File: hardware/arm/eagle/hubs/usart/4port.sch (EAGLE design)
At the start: 15 parts

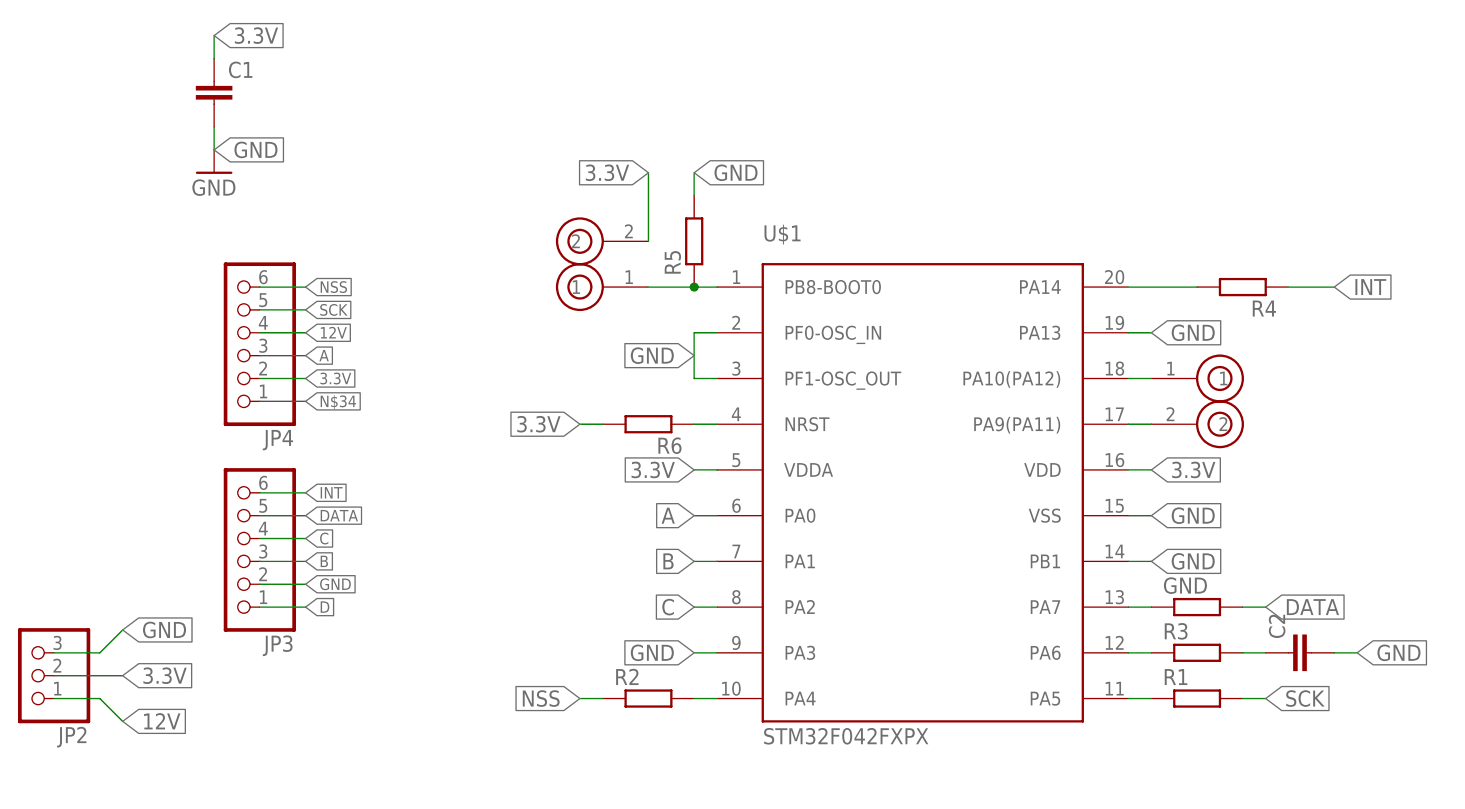
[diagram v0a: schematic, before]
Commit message: updated uart hub pcb
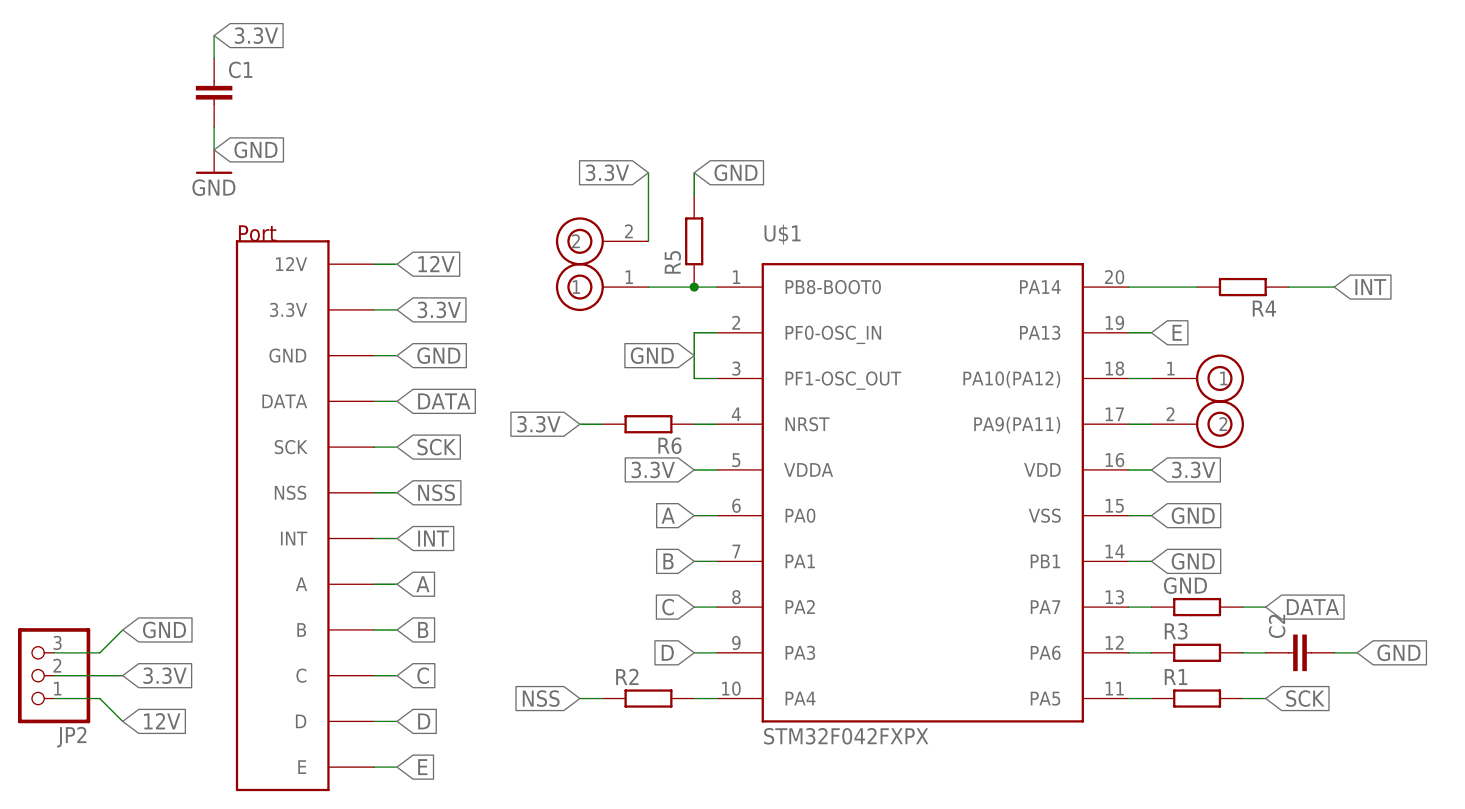
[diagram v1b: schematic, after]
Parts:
- removed JP3, JP4: (no value), pinhead:PINHD-1X6
- added U$4: HUB_PORT, gumyns:HUB_PORT
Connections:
- removed net N$34: JP4.1
- new net E: U$1.PA13, U$4.E
- net 12V: now also U$4.12V; no longer JP4.4
- net 3.3V: now also U$4.3.3V; no longer JP4.2
- net A: now also U$4.A; no longer JP4.3
- net B: now also U$4.B; no longer JP3.3
- net C: now also U$4.C; no longer JP3.4
- net D: now also U$1.PA3, U$4.D; no longer JP3.1
- net DATA: now also U$4.DATA; no longer JP3.5
- net GND: now also U$4.GND; no longer JP3.2, U$1.PA13, U$1.PA3
- net INT: now also U$4.INT; no longer JP3.6
- net NSS: now also U$4.NSS; no longer JP4.6
- net SCK: now also U$4.SCK; no longer JP4.5
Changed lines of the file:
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@@
 <?xml version="1.0" encoding="utf-8"?>
 <!DOCTYPE eagle SYSTEM "eagle.dtd">
-<eagle version="7.7.0">
+<eagle version="7.6.0">
 <drawing>
 <settings>
@@
 <part name="C2" library="resistor" deviceset="C-EU" device="C1206"/>
 <part name="R4" library="resistor" deviceset="R-EU_" device="R0603"/>
-<part name="JP3" library="pinhead" deviceset="PINHD-1X6" device=""/>
-<part name="JP4" library="pinhead" deviceset="PINHD-1X6" device=""/>
+<part name="U$4" library="gumyns" deviceset="HUB_PORT" device=""/>
 </parts>
 <sheets>
@@
 <instance part="C2" gate="G$1" x="142.24" y="63.5" rot="R90"/>
 <instance part="R4" gate="G$1" x="137.16" y="104.14" rot="R180"/>
-<instance part="JP3" gate="A" x="25.4" y="76.2" rot="R180"/>
-<instance part="JP4" gate="A" x="25.4" y="99.06" rot="R180"/>
+<instance part="U$4" gate="G$2" x="33.02" y="76.2"/>
 </instances>
 <busses>
@@
 </segment>
 <segment>
-<pinref part="JP4" gate="A" pin="4"/>
-<wire x1="27.94" y1="99.06" x2="33.02" y2="99.06" width="0.1524" layer="91"/>
-<label x="33.02" y="99.06" size="1.27" layer="95" xref="yes"/>
+<pinref part="U$4" gate="G$2" pin="12V"/>
+<wire x1="40.64" y1="106.68" x2="43.18" y2="106.68" width="0.1524" layer="91"/>
+<label x="43.18" y="106.68" size="1.778" layer="95" xref="yes"/>
 </segment>
 </net>
@@
 </segment>
 <segment>
-<pinref part="JP4" gate="A" pin="2"/>
-<wire x1="27.94" y1="93.98" x2="33.02" y2="93.98" width="0.1524" layer="91"/>
-<label x="33.02" y="93.98" size="1.27" layer="95" xref="yes"/>
+<pinref part="U$4" gate="G$2" pin="3.3V"/>
+<wire x1="40.64" y1="101.6" x2="43.18" y2="101.6" width="0.1524" layer="91"/>
+<label x="43.18" y="101.6" size="1.778" layer="95" xref="yes"/>
 </segment>
 </net>
@@
 </segment>
 <segment>
-<pinref part="U$1" gate="G$1" pin="PA13"/>
-<wire x1="124.46" y1="99.06" x2="127" y2="99.06" width="0.1524" layer="91"/>
-<label x="127" y="99.06" size="1.778" layer="95" xref="yes"/>
-</segment>
-<segment>
 <pinref part="U$1" gate="G$1" pin="VSS"/>
 <wire x1="124.46" y1="78.74" x2="127" y2="78.74" width="0.1524" layer="91"/>
@@
 </segment>
 <segment>
-<pinref part="U$1" gate="G$1" pin="PA3"/>
-<wire x1="78.74" y1="63.5" x2="76.2" y2="63.5" width="0.1524" layer="91"/>
-<label x="76.2" y="63.5" size="1.778" layer="95" rot="R180" xref="yes"/>
-</segment>
-<segment>
 <pinref part="R5" gate="G$1" pin="2"/>
 <wire x1="76.2" y1="114.3" x2="76.2" y2="116.84" width="0.1524" layer="91"/>
@@
 </segment>
 <segment>
-<pinref part="JP3" gate="A" pin="2"/>
-<wire x1="27.94" y1="71.12" x2="33.02" y2="71.12" width="0.1524" layer="91"/>
-<label x="33.02" y="71.12" size="1.27" layer="95" xref="yes"/>
+<pinref part="U$4" gate="G$2" pin="GND"/>
+<wire x1="40.64" y1="96.52" x2="43.18" y2="96.52" width="0.1524" layer="91"/>
+<label x="43.18" y="96.52" size="1.778" layer="95" xref="yes"/>
 </segment>
 </net>
@@
 </segment>
 <segment>
-<pinref part="JP4" gate="A" pin="6"/>
-<wire x1="27.94" y1="104.14" x2="33.02" y2="104.14" width="0.1524" layer="91"/>
-<label x="33.02" y="104.14" size="1.27" layer="95" xref="yes"/>
+<pinref part="U$4" gate="G$2" pin="NSS"/>
+<wire x1="40.64" y1="81.28" x2="43.18" y2="81.28" width="0.1524" layer="91"/>
+<label x="43.18" y="81.28" size="1.778" layer="95" xref="yes"/>
 </segment>
 </net>
@@
 </segment>
 <segment>
-<pinref part="JP3" gate="A" pin="6"/>
-<wire x1="27.94" y1="81.28" x2="33.02" y2="81.28" width="0.1524" layer="91"/>
-<label x="33.02" y="81.28" size="1.27" layer="95" xref="yes"/>
+<pinref part="U$4" gate="G$2" pin="INT"/>
+<wire x1="40.64" y1="76.2" x2="43.18" y2="76.2" width="0.1524" layer="91"/>
+<label x="43.18" y="76.2" size="1.778" layer="95" xref="yes"/>
 </segment>
 </net>
@@
 </segment>
 <segment>
-<pinref part="JP4" gate="A" pin="5"/>
-<wire x1="27.94" y1="101.6" x2="33.02" y2="101.6" width="0.1524" layer="91"/>
-<label x="33.02" y="101.6" size="1.27" layer="95" xref="yes"/>
+<pinref part="U$4" gate="G$2" pin="SCK"/>
+<wire x1="40.64" y1="86.36" x2="43.18" y2="86.36" width="0.1524" layer="91"/>
+<label x="43.18" y="86.36" size="1.778" layer="95" xref="yes"/>
 </segment>
 </net>
@@
 </segment>
 <segment>
-<pinref part="JP3" gate="A" pin="5"/>
-<wire x1="27.94" y1="78.74" x2="33.02" y2="78.74" width="0.1524" layer="91"/>
-<label x="33.02" y="78.74" size="1.27" layer="95" xref="yes"/>
+<pinref part="U$4" gate="G$2" pin="DATA"/>
+<wire x1="40.64" y1="91.44" x2="43.18" y2="91.44" width="0.1524" layer="91"/>
+<label x="43.18" y="91.44" size="1.778" layer="95" xref="yes"/>
 </segment>
 </net>
@@
 </segment>
 <segment>
-<pinref part="JP4" gate="A" pin="3"/>
-<wire x1="27.94" y1="96.52" x2="33.02" y2="96.52" width="0.1524" layer="91"/>
-<label x="33.02" y="96.52" size="1.27" layer="95" xref="yes"/>
+<pinref part="U$4" gate="G$2" pin="A"/>
+<wire x1="40.64" y1="71.12" x2="43.18" y2="71.12" width="0.1524" layer="91"/>
+<label x="43.18" y="71.12" size="1.778" layer="95" xref="yes"/>
 </segment>
 </net>
@@
 </segment>
 <segment>
-<pinref part="JP3" gate="A" pin="3"/>
-<wire x1="27.94" y1="73.66" x2="33.02" y2="73.66" width="0.1524" layer="91"/>
-<label x="33.02" y="73.66" size="1.27" layer="95" xref="yes"/>
+<pinref part="U$4" gate="G$2" pin="B"/>
+<wire x1="40.64" y1="66.04" x2="43.18" y2="66.04" width="0.1524" layer="91"/>
+<label x="43.18" y="66.04" size="1.778" layer="95" xref="yes"/>
 </segment>
 </net>
@@
 </segment>
 <segment>
-<pinref part="JP3" gate="A" pin="4"/>
-<wire x1="27.94" y1="76.2" x2="33.02" y2="76.2" width="0.1524" layer="91"/>
-<label x="33.02" y="76.2" size="1.27" layer="95" xref="yes"/>
+<pinref part="U$4" gate="G$2" pin="C"/>
+<wire x1="40.64" y1="60.96" x2="43.18" y2="60.96" width="0.1524" layer="91"/>
+<label x="43.18" y="60.96" size="1.778" layer="95" xref="yes"/>
 </segment>
 </net>
@@
 </segment>
 </net>
-<net name="N$34" class="0">
-<segment>
-<pinref part="JP4" gate="A" pin="1"/>
-<wire x1="27.94" y1="91.44" x2="33.02" y2="91.44" width="0.1524" layer="91"/>
-<label x="33.02" y="91.44" size="1.27" layer="95" xref="yes"/>
-</segment>
-</net>
 <net name="D" class="0">
 <segment>
-<pinref part="JP3" gate="A" pin="1"/>
-<wire x1="27.94" y1="68.58" x2="33.02" y2="68.58" width="0.1524" layer="91"/>
-<label x="33.02" y="68.58" size="1.27" layer="95" xref="yes"/>
-</segment>
-</net>
+<pinref part="U$4" gate="G$2" pin="D"/>
+<wire x1="40.64" y1="55.88" x2="43.18" y2="55.88" width="0.1524" layer="91"/>
+<label x="43.18" y="55.88" size="1.778" layer="95" xref="yes"/>
+</segment>
+<segment>
+<pinref part="U$1" gate="G$1" pin="PA3"/>
+<wire x1="78.74" y1="63.5" x2="76.2" y2="63.5" width="0.1524" layer="91"/>
+<label x="76.2" y="63.5" size="1.778" layer="95" rot="R180" xref="yes"/>
+</segment>
+</net>
+<net name="E" class="0">
+<segment>
+<pinref part="U$4" gate="G$2" pin="E"/>
+<wire x1="40.64" y1="50.8" x2="43.18" y2="50.8" width="0.1524" layer="91"/>
+<label x="43.18" y="50.8" size="1.778" layer="95" xref="yes"/>
+</segment>
+<segment>
+<pinref part="U$1" gate="G$1" pin="PA13"/>
+<wire x1="124.46" y1="99.06" x2="127" y2="99.06" width="0.1524" layer="91"/>
+<label x="127" y="99.06" size="1.778" layer="95" xref="yes"/>
+</segment>
+</net>
